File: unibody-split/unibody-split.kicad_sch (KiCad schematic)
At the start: 95 parts, among them IC1 AP130-20, SW1 SW_Push, SW10 SW_Push, SW11 SW_Push, SW12 SW_Push, SW13 SW_Push, SW14 SW_Push, SW15 SW_Push, SW16 SW_Push, SW17 SW_Push, SW18 SW_Push, SW19 SW_Push, SW2 SW_Push, SW20 SW_Push, SW21 SW_Push, SW22 SW_Push, SW23 SW_Push, SW24 SW_Push, SW25 SW_Push, SW26 SW_Push, SW27 SW_Push, SW28 SW_Push, SW29 SW_Push, SW3 SW_Push, SW30 SW_Push, SW31 SW_Push, SW32 SW_Push, SW33 SW_Push, SW34 SW_Push, SW35 SW_Push, SW36 SW_Push, SW37 SW_Push, SW38 SW_Push, SW39 SW_Push, SW4 SW_Push, SW40 SW_Push, SW41 SW_Push, SW42 SW_Push, SW5 SW_Push, SW6 SW_Push, SW7 SW_Push, SW8 SW_Push, SW9 SW_Push, U1 Pico, U2 PMW3360DM-T2QU, U3 HackPackv4-rescue:PSP_1000_JS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

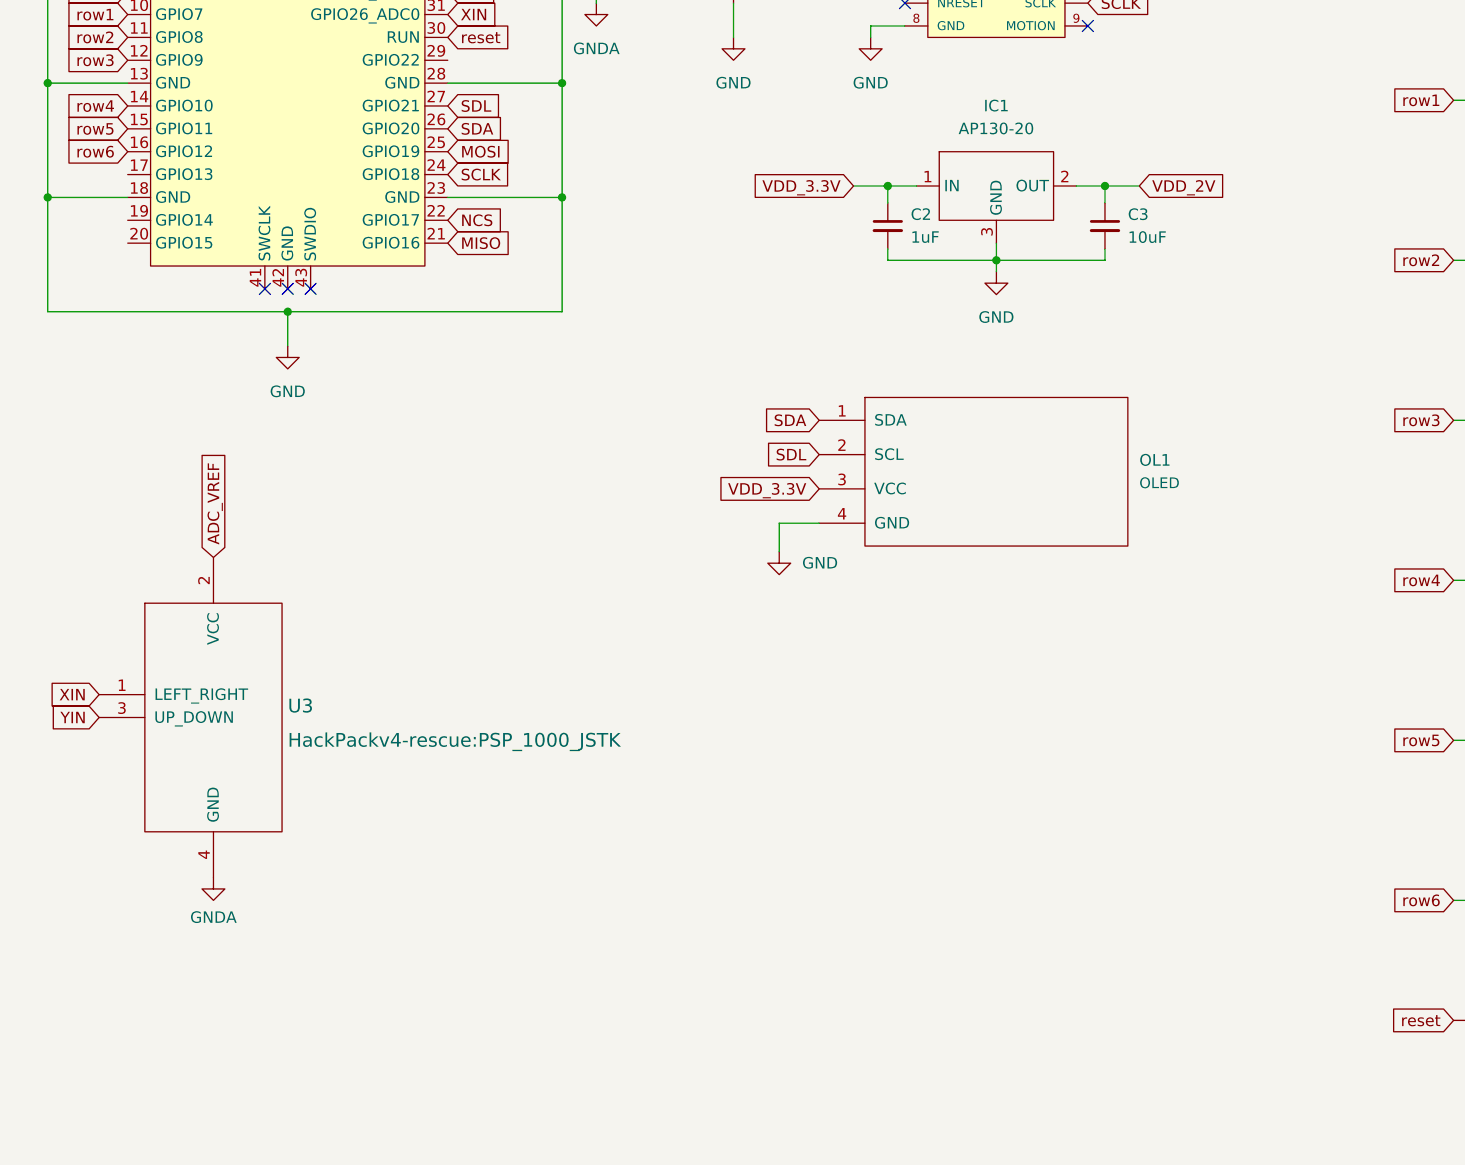
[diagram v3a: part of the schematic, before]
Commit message: Added two more analog sticks
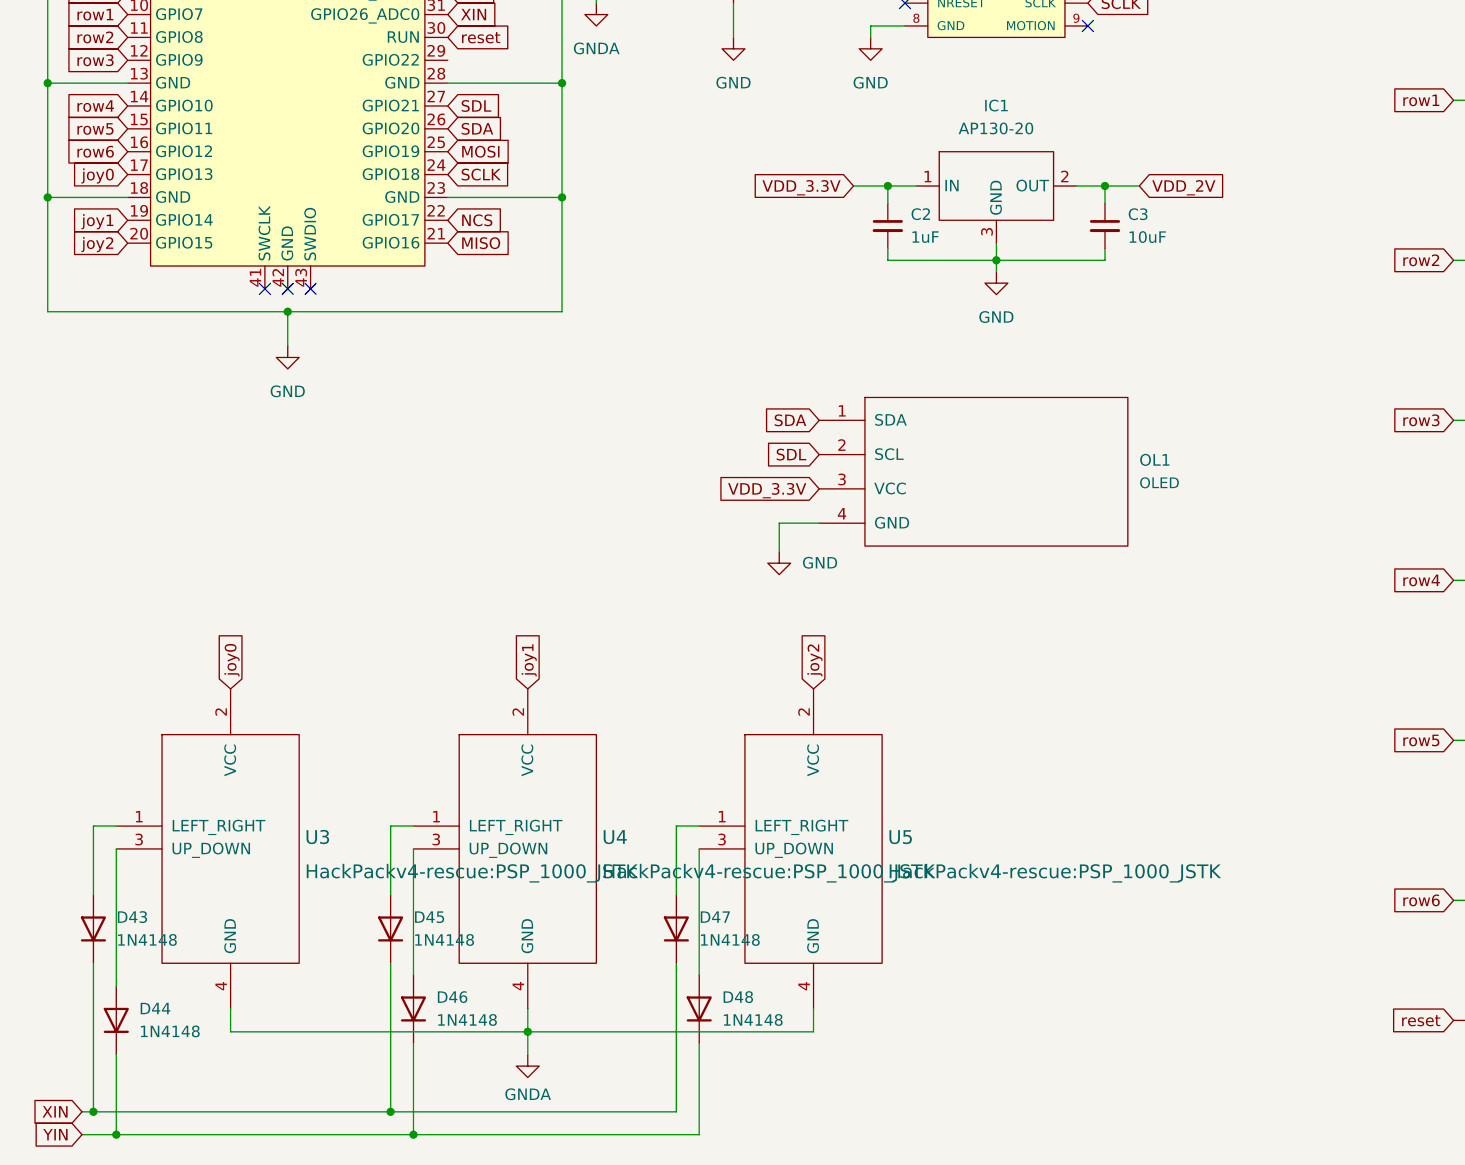
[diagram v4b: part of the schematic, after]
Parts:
- added D43, D44, D45, D46, D47, D48: 1N4148, Diode_THT:D_DO-35_SOD27_P7.62mm_Horizontal, symbol Diode:1N4148
- added U4, U5: HackPackv4-rescue:PSP_1000_JSTK, HackPack_Footprints:JOYSTICK-PSP1000, symbol HackPackv4-cache:HackPackv4-rescue{colon}PSP_1000_JSTK
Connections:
- net ADC_VREF: no longer U3.2 (VCC)
- net GNDA: now also U4.4 (GND), U5.4 (GND)
- net XIN: now also D43.1 (K), D45.1 (K), D47.1 (K); no longer U3.1 (LEFT_RIGHT)
- net YIN: now also D44.1 (K), D46.1 (K), D48.1 (K); no longer U3.3 (UP_DOWN)
- net joy0: now reaches U1.17 (GPIO13)
- net joy0: now also U3.2 (VCC)
- net joy1: now reaches U1.19 (GPIO14)
- net joy1: now also U4.2 (VCC)
- net joy2: now reaches U1.20 (GPIO15)
- net joy2: now also U5.2 (VCC)
- new net: D43.2 (A), U3.1 (LEFT_RIGHT)
- new net: D44.2 (A), U3.3 (UP_DOWN)
- new net: D45.2 (A), U4.1 (LEFT_RIGHT)
- new net: D46.2 (A), U4.3 (UP_DOWN)
- new net: D47.2 (A), U5.1 (LEFT_RIGHT)
- new net: D48.2 (A), U5.3 (UP_DOWN)
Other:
- moved on the sheet: U3

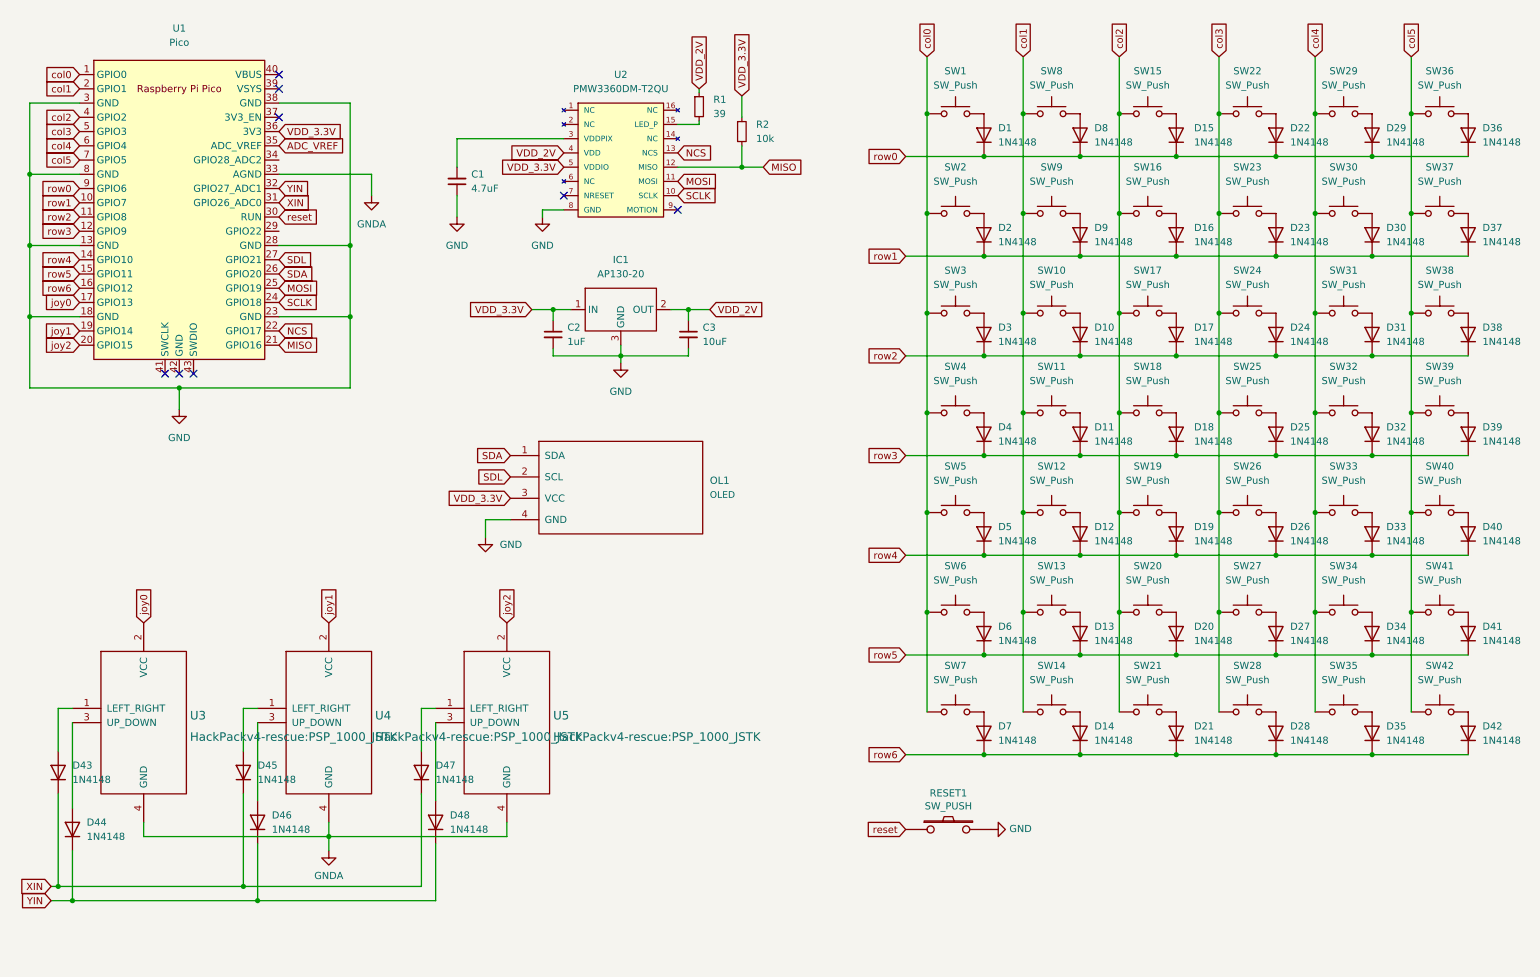
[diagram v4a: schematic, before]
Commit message: Removed RPi-Pico debug pins, Updated PCB to contain 3 joysticks
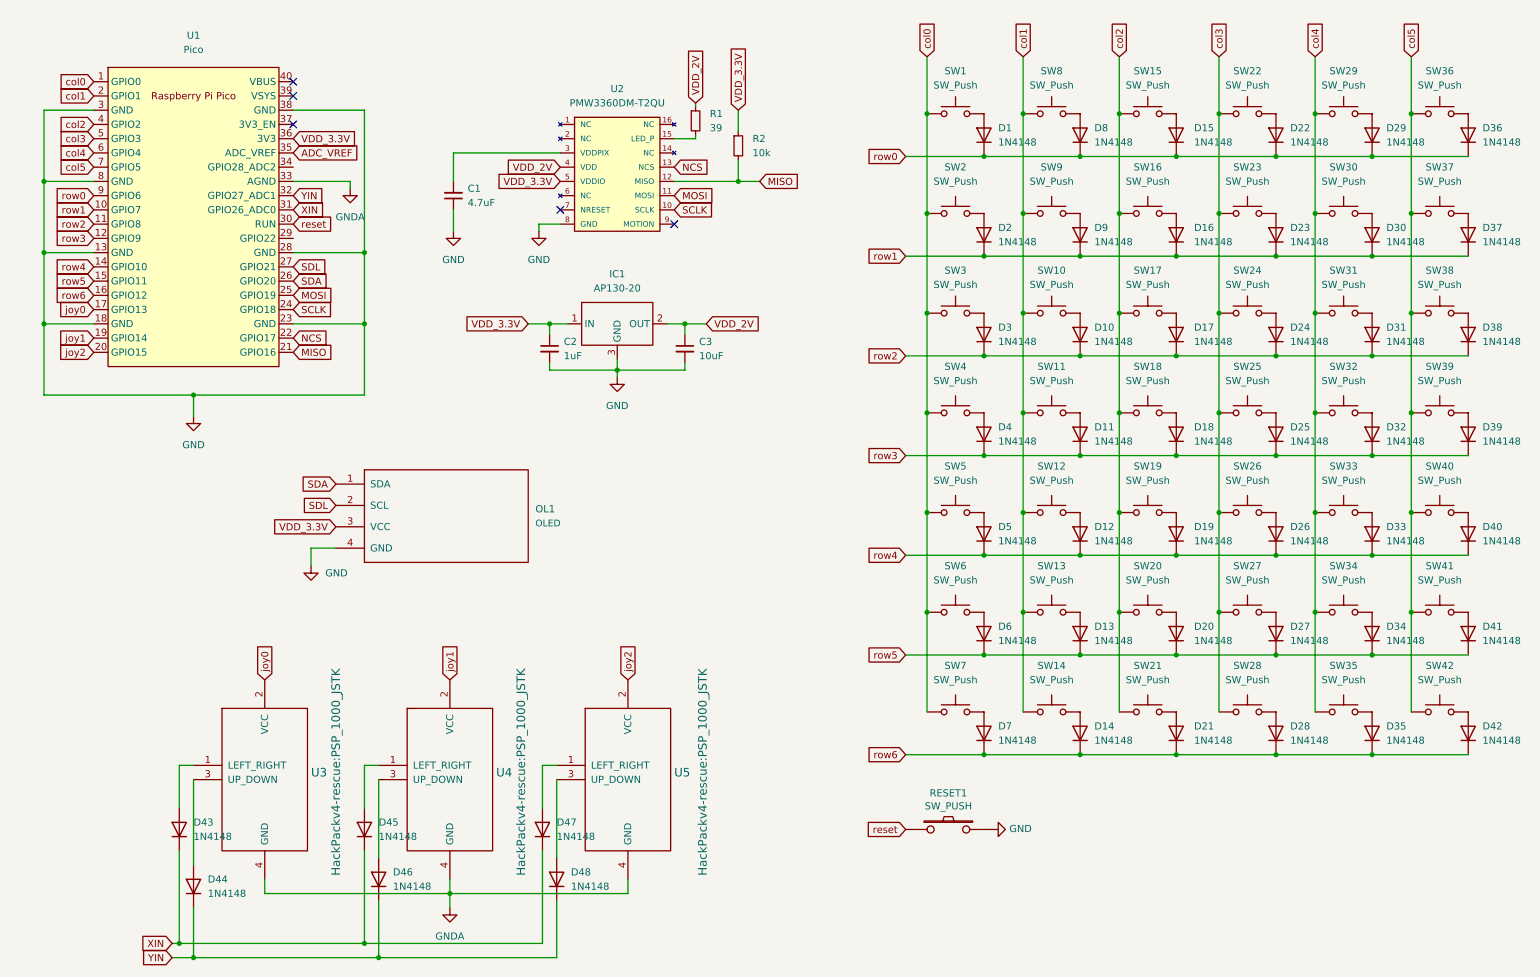
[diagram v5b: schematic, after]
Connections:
- no-connect marks 8 -> 5
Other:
- moved on the sheet: C1, C2, C3, D43, D44, D45, D46, D47, D48, IC1, OL1, R1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

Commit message: Done routing PCB
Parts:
- D1, D10, D11, D12, D13, D14, D15, D16, D17, D18, D19, D2, D20, D21, D22, D23, D24, D25, D26, D27, D28, D29, D3, D30, D31, D32, D33, D34, D35, D36, D37, D38, D39, D4, D40, D41, D42, D43, D44, D45, D46, D47, D48, D5, D6, D7, D8, D9: footprint Diode_THT:D_DO-35_SOD27_P7.62mm_Horizontal -> unibody-split:D_DO-35_SOD27_P7.62mm_Horizontal
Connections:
- net GND: now also U3.4 (GND), U4.4 (GND), U5.4 (GND)
- net GNDA: no longer U3.4 (GND), U4.4 (GND), U5.4 (GND)
- net ADC_VREF: no longer names the net of U1.35 (ADC_VREF)
- no-connect marks 5 -> 8

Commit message: Updated PCB routing, added thread holes
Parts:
- OL1: footprint kbd:OLED_v2 -> unibody-split:OLED_v2
- RESET1: footprint Button_Switch_SMD:SW_SPST_B3U-1000P -> Button_Switch_SMD:SW_SPST_CK_RS282G05A3
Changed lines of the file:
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@@
     (property "Reference" "RESET1" (id 0) (at 180.34 152.273 0))
     (property "Value" "SW_PUSH" (id 1) (at 180.34 154.5844 0))
-    (property "Footprint" "Button_Switch_SMD:SW_SPST_B3U-1000P" (id 2) (at 180.34 158.75 0)
+    (property "Footprint" "Button_Switch_SMD:SW_SPST_CK_RS282G05A3" (id 2) (at 180.34 158.75 0)
       (effects (font (size 1.27 1.27)) hide)
     )
@@
       (effects (font (size 1.1938 1.1938)) (justify left))
     )
-    (property "Footprint" "kbd:OLED_v2" (id 2) (at 90.17 100.965 0)
+    (property "Footprint" "unibody-split:OLED_v2" (id 2) (at 90.17 100.965 0)
       (effects (font (size 1.524 1.524)) hide)
     )
@@
     )
     (path "/a8e7698b-c7a7-47cb-a0b9-26cf74a23d1b"
-      (reference "OL1") (unit 1) (value "OLED") (footprint "kbd:OLED_v2")
+      (reference "OL1") (unit 1) (value "OLED") (footprint "unibody-split:OLED_v2")
     )
     (path "/680a68fc-2ed0-45fc-8a97-39ab1f619573"
@@
     )
     (path "/7ea9b7cb-8f63-42a2-bb9d-0ae9b9f5fa5b"
-      (reference "RESET1") (unit 1) (value "SW_PUSH") (footprint "Button_Switch_SMD:SW_SPST_B3U-1000P")
+      (reference "RESET1") (unit 1) (value "SW_PUSH") (footprint "Button_Switch_SMD:SW_SPST_CK_RS282G05A3")
     )
     (path "/61af01d5-7163-43c5-ad16-3a7bdac0b9e9"
